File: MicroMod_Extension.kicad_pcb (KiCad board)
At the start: 4 copper layers, 38.4 x 38.4 mm, 79 parts, among them J1 2199230-4, J10 Conn_01x02, J2 XKB_U262-16XN-4BVC11, J3 RSP-122811-01, J4 Screw_Terminal_01x04, J5 Conn_01x08, J6 Conn_01x08, J7 Conn_01x04, J8 Conn_01x04, J9 Conn_01x04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

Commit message: submission
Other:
- board text added: ">"
- board text added: "POD.110621"

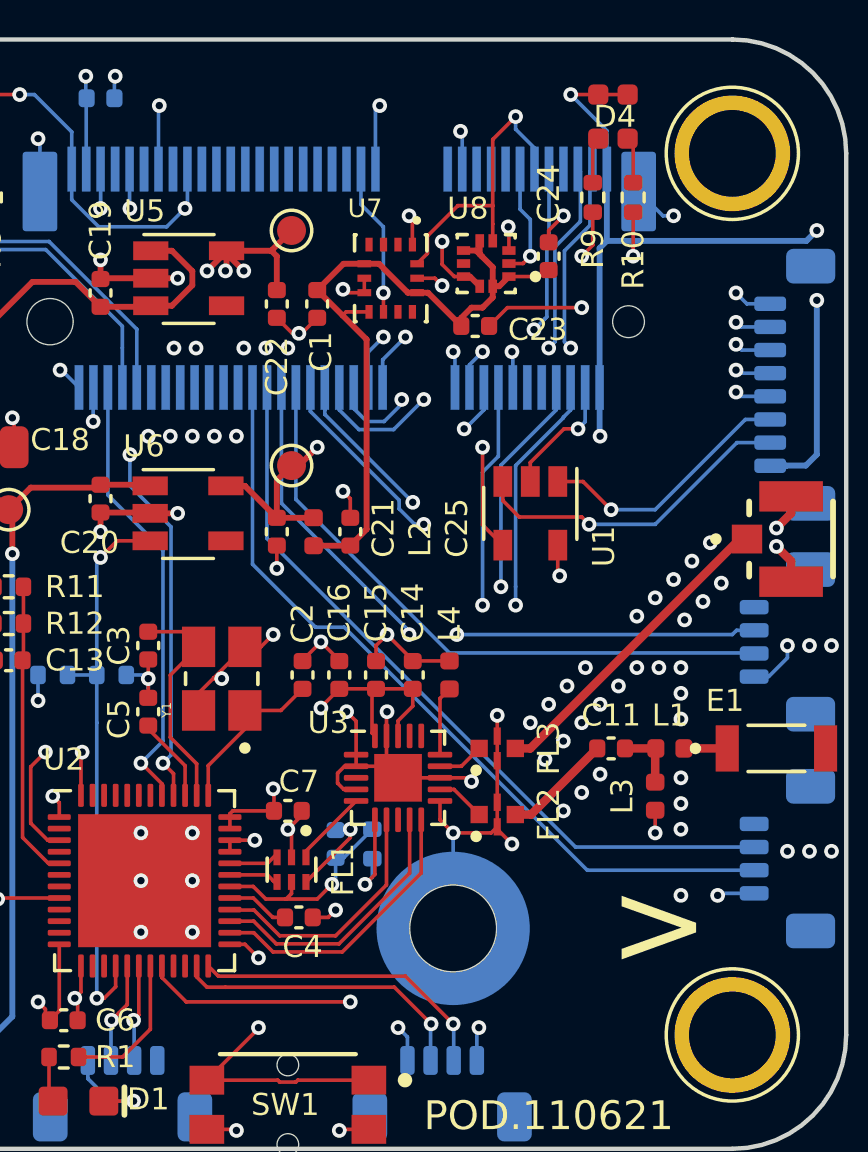
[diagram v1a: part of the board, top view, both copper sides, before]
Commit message: fix bmp384 footprint
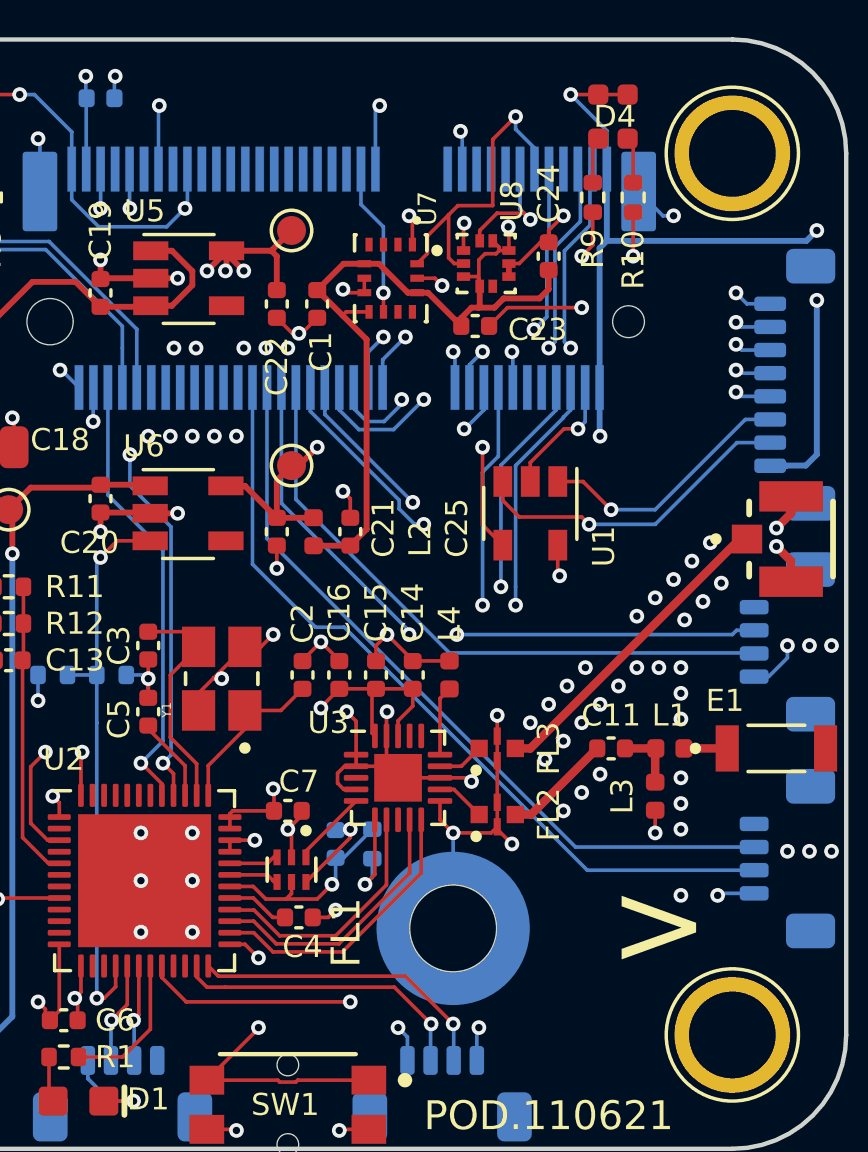
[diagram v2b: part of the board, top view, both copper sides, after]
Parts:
- turned U8 to 0 degrees
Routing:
- net /VCCI: track 24.9 -> 27.5 mm, vias 0 -> 1
- net /IMU_SCL: track 8.74 -> 10.3 mm
- net /IMU_SDA: track 10.5 -> 11.4 mm
- net GND: track 118.2 -> 118.1 mm, vias 115 -> 114

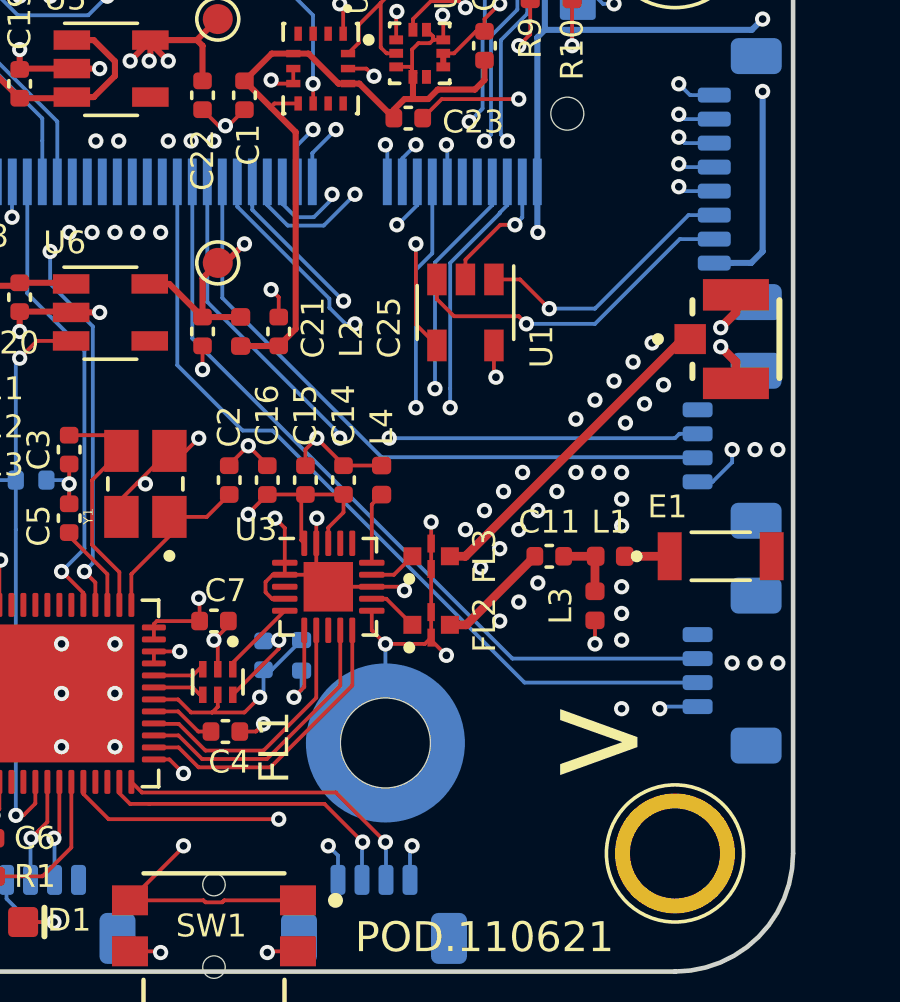
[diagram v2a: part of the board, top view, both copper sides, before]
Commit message: fix screw position
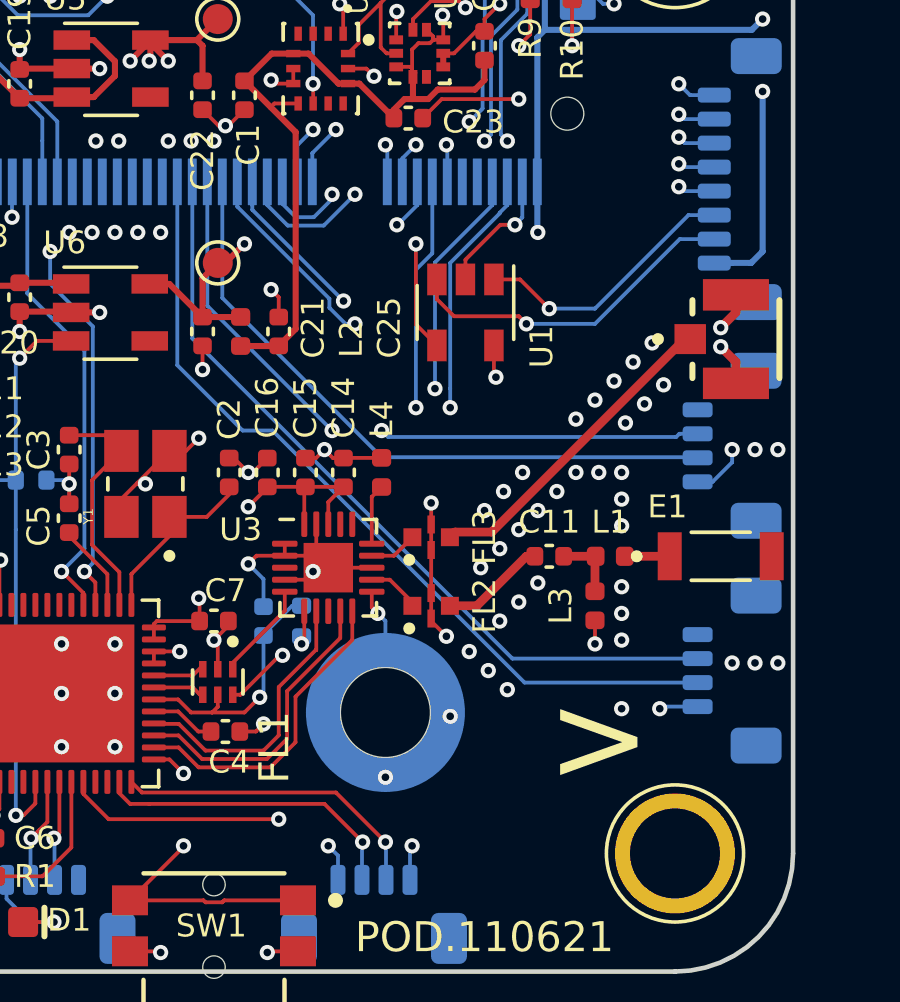
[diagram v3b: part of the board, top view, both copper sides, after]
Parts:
- moved C17 1.14 mm to (146.3, 71.0)
- moved R13 1.14 mm to (147.6, 71.0)
- moved TP8 1.02 mm to (150.4, 74.0)
- moved FL2 0.64 mm to (151.9, 70.5)
- moved FL3 0.64 mm to (151.9, 68.2)
- moved U3 0.63 mm to (148.5, 69.2)
- moved C14 0.25 mm to (149.0, 66.0)
- moved C15 0.25 mm to (147.7, 66.0)
- moved C16 0.25 mm to (146.4, 66.0)
- moved C2 0.25 mm to (145.2, 66.0)
- moved L4 0.25 mm to (150.2, 66.0)
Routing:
- net GND: track 118.1 -> 113.9 mm, vias 114 -> 117
- net Net-(R13-Pad2): track 3.37 -> 1.38 mm
- net Net-(C17-Pad2): track 7.28 -> 8.44 mm
- net /VCC_NRF: track 25.6 -> 24.9 mm
- net /PA_RXEN: track 8.77 -> 9.41 mm
- net Net-(FL1-Pad1): track 2.67 -> 3.30 mm
- net /PA_MODE: track 9.40 -> 10.0 mm
- net /PA_SW_ANT: track 9.86 -> 10.5 mm

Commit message: update pcb
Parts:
- added ?: , , B.Cu at (129.3, 54.4)
- added ?: , , B.Cu at (160.1, 59.2)
- added J11: Screw_Terminal_01x04, Connector_JST:JST_SUR_SM04B-SURS-TF_1x04-1MP_P0.80mm_Horizontal, F.Cu at (143.8, 46.2)
- C12: moved to F.Cu
- moved D5 19.9 mm to (133.7, 57.7), turned to 270 degrees
- moved C12 9.12 mm to (128.4, 63.1), turned to 180 degrees
- moved J10 5.12 mm to (129.8, 54.9), turned to 90 degrees
- moved R14 2.33 mm to (132.8, 59.7), turned to 90 degrees
- moved L5 1.55 mm to (131.6, 57.3)
- moved C18 1.37 mm to (135.4, 57.7)
- moved R15 1.20 mm to (132.8, 61.8)
- moved TP1 0.38 mm to (135.4, 60.6)
- moved C24 0.18 mm to (153.5, 51.7), turned to 90 degrees
- renumbered E1 to <E1
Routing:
- net Net-(C18-Pad2): track 47.0 -> 32.9 mm
- net /STM_SWIO: track 0.00 -> 6.61 mm, vias 0 -> 1
- net /STM_SWCLK: track 0.00 -> 5.94 mm, vias 0 -> 1
- net /VCC: track 74.6 -> 80.3 mm
- net VBUS: track 47.0 -> 50.0 mm
- net Net-(L5-Pad2): track 4.42 -> 2.38 mm
- net GND: track 113.9 -> 111.9 mm, vias 117 -> 120
- net /VCCI: track 27.5 -> 25.5 mm
- net Net-(R14-Pad1): track 3.55 -> 2.66 mm
- net /PM_PGOOD: track 23.1 -> 22.4 mm
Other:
- board text added: "+"
- board text added: "FLOW&H"
- board text added: "I<"
- board text added: "MOTORS"
- board text added: "NRF"
- board text added: "NRF_U2"
- board text added: "POD.111621"
- board text added: "STM"
- board text added: "STM_U1"
- board text added: "STM_U2"
- board text removed: "POD.110621"

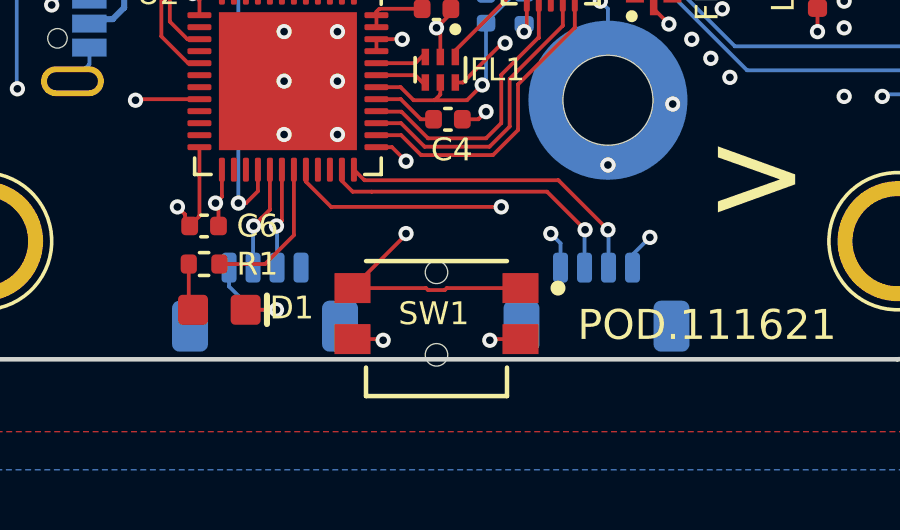
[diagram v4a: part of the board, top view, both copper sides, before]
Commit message: fix switch position
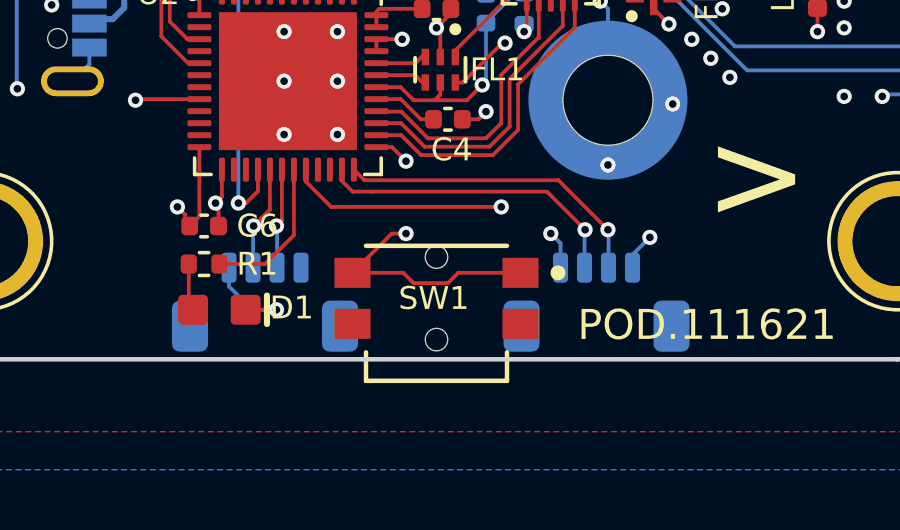
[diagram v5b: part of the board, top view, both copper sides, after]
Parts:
- moved SW1 0.51 mm to (144.7, 80.6)
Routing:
- net GND: track 111.9 -> 109.9 mm, vias 120 -> 118

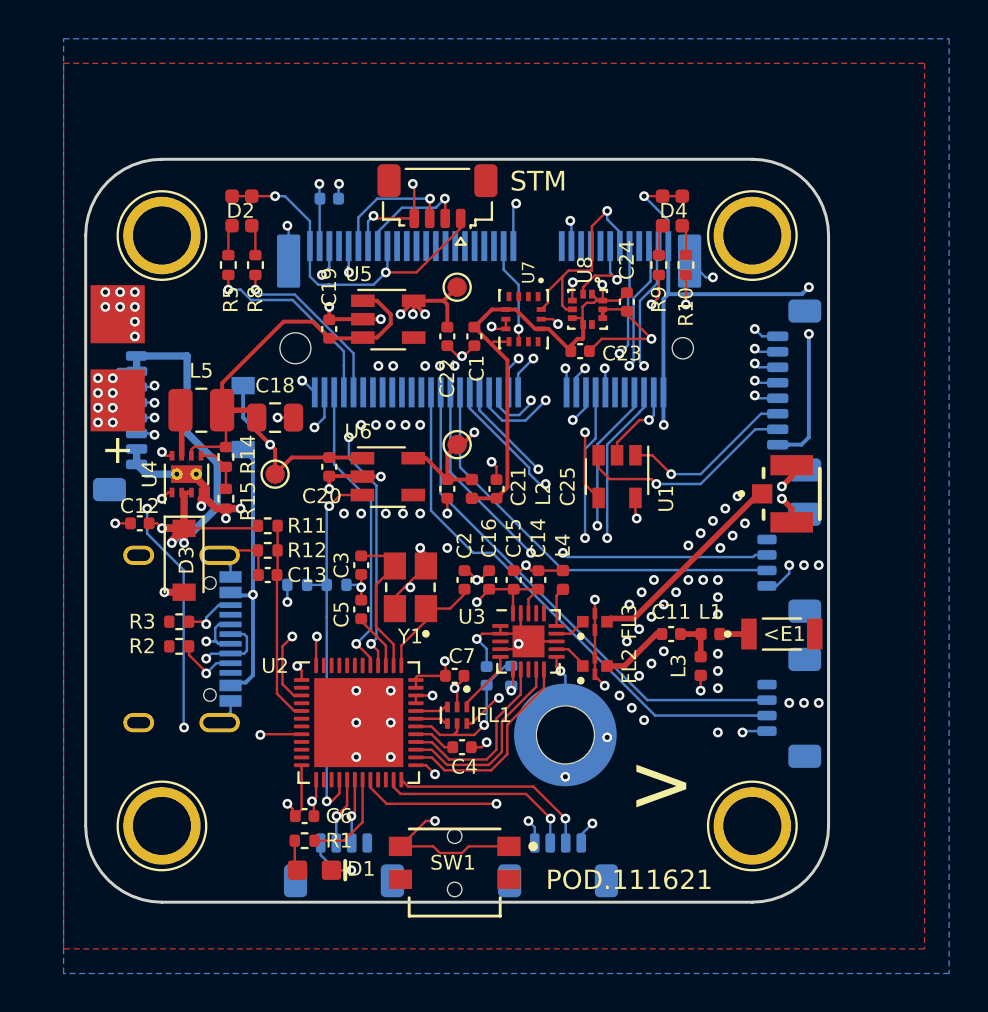
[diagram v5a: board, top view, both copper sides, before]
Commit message: change motor2 and motor4
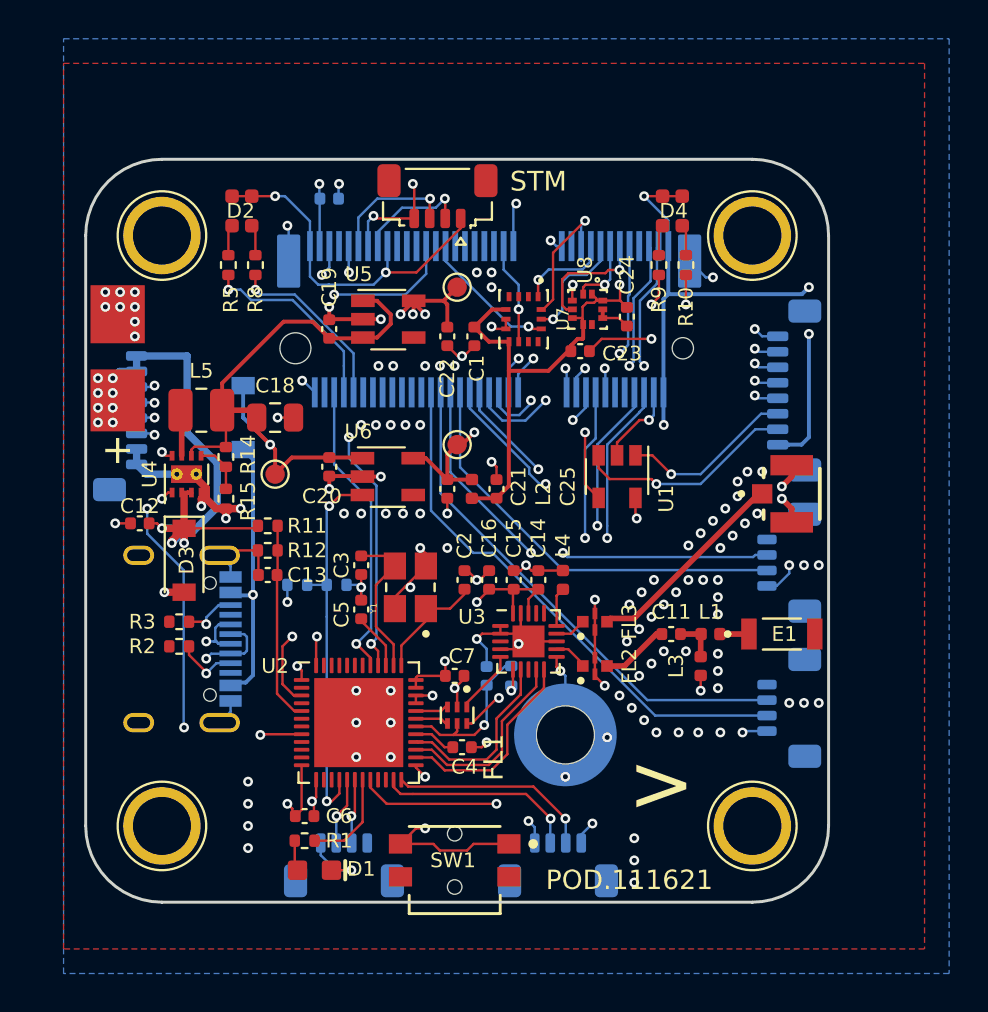
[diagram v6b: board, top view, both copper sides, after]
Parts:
- removed ? (x2): , 
- R1, R10, R5, R8, R9: value 150r -> 1k
- moved C24 0.76 mm to (153.5, 52.5)
- moved SW1 0.13 mm to (144.7, 80.5)
- renumbered <E1 to E1
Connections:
- J1 pad 21: /MOTOR2 -> /B11
- J1 pad 23: /B10 -> /MOTOR2
- J1 pad 51: /B8 -> /MOTOR4
- J1 pad 72: /MOTOR4 -> /B9
- U7 pad 1: GND -> /SPI2_MISO
- U7 pad 12: /VCCI -> /C13
- U7 pad 13: /IMU_SCL -> /SPI2_SCK
- U7 pad 14: /IMU_SDA -> /SPI2_MOSI
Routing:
- net /MOTOR4: track 11.4 -> 19.9 mm
- net /SPI2_MOSI: track 0.00 -> 7.74 mm, vias 0 -> 1
- net /C13: track 0.00 -> 7.16 mm, vias 0 -> 1
- net /IMU_SCL: track 10.3 -> 3.64 mm, vias 2 -> 1
- net /SPI2_SCK: track 0.00 -> 5.93 mm, vias 0 -> 1
- net /IMU_SDA: track 11.4 -> 6.39 mm
- net /SPI2_MISO: track 0.00 -> 4.76 mm, vias 0 -> 1
- net /MOTOR2: track 28.9 -> 26.3 mm
- net GND: track 109.9 -> 108.0 mm, vias 118 -> 136
- net /VCCI: track 25.5 -> 24.6 mm
- net /SWITCH: track 11.8 -> 11.0 mm
